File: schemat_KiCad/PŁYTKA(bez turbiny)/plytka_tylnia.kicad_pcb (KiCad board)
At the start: 2 copper layers, 200 x 150 mm, 80 parts, among them J1 CONN_01X04, J2 CONN_01X04, J3 CONN_01X04, J4 CONN_01X04, J5 CONN_01X04, J6 CONN_01X04, J7 PIN10, J8 CONN_01X04, J9 CONN_01X04, P1 USB_OTG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

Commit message: poprawiona, odchudzona, zaokraglona
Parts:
- moved R19 179.7 mm to (45.5, 65.0), turned to 90 degrees
- moved T5 179.7 mm to (45.5, 65.0), turned to 90 degrees
- moved R11 173.6 mm to (50.5, 68.0), turned to 90 degrees
- moved R15 160.5 mm to (60.5, 70.0), turned to 90 degrees
- moved T1 160.5 mm to (60.5, 70.0), turned to 90 degrees
- moved R1 154.0 mm to (66.0, 72.5), turned to 90 degrees
- moved R20 141.1 mm to (75.5, 72.5), turned to 90 degrees
- moved T6 141.1 mm to (75.5, 72.5), turned to 90 degrees
- moved J6 137.0 mm to (161.8, 163.2), turned to 0 degrees
- moved R12 136.3 mm to (80.0, 75.0), turned to 90 degrees
- moved C1.2 131.0 mm to (169.0, 158.8), turned to 270 degrees
- moved R16 127.1 mm to (89.0, 79.6), turned to 90 degrees
- moved U1 126.4 mm to (164.3, 155.7), turned to 270 degrees
- moved C15 123.7 mm to (169.0, 153.6), turned to 90 degrees
- moved T2 122.5 mm to (90.5, 75.0), turned to 90 degrees
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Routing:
- net GND: track 333.4 -> 356.9 mm, vias 5 -> 4
- net /GND1: track 84.5 -> 70.2 mm
- net /T2: track 70.0 -> 74.1 mm, vias 0 -> 1
- net /T1: track 95.3 -> 93.6 mm
- net VCC: track 569.1 -> 570.7 mm
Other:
- outline, holes or cut-outs redrawn

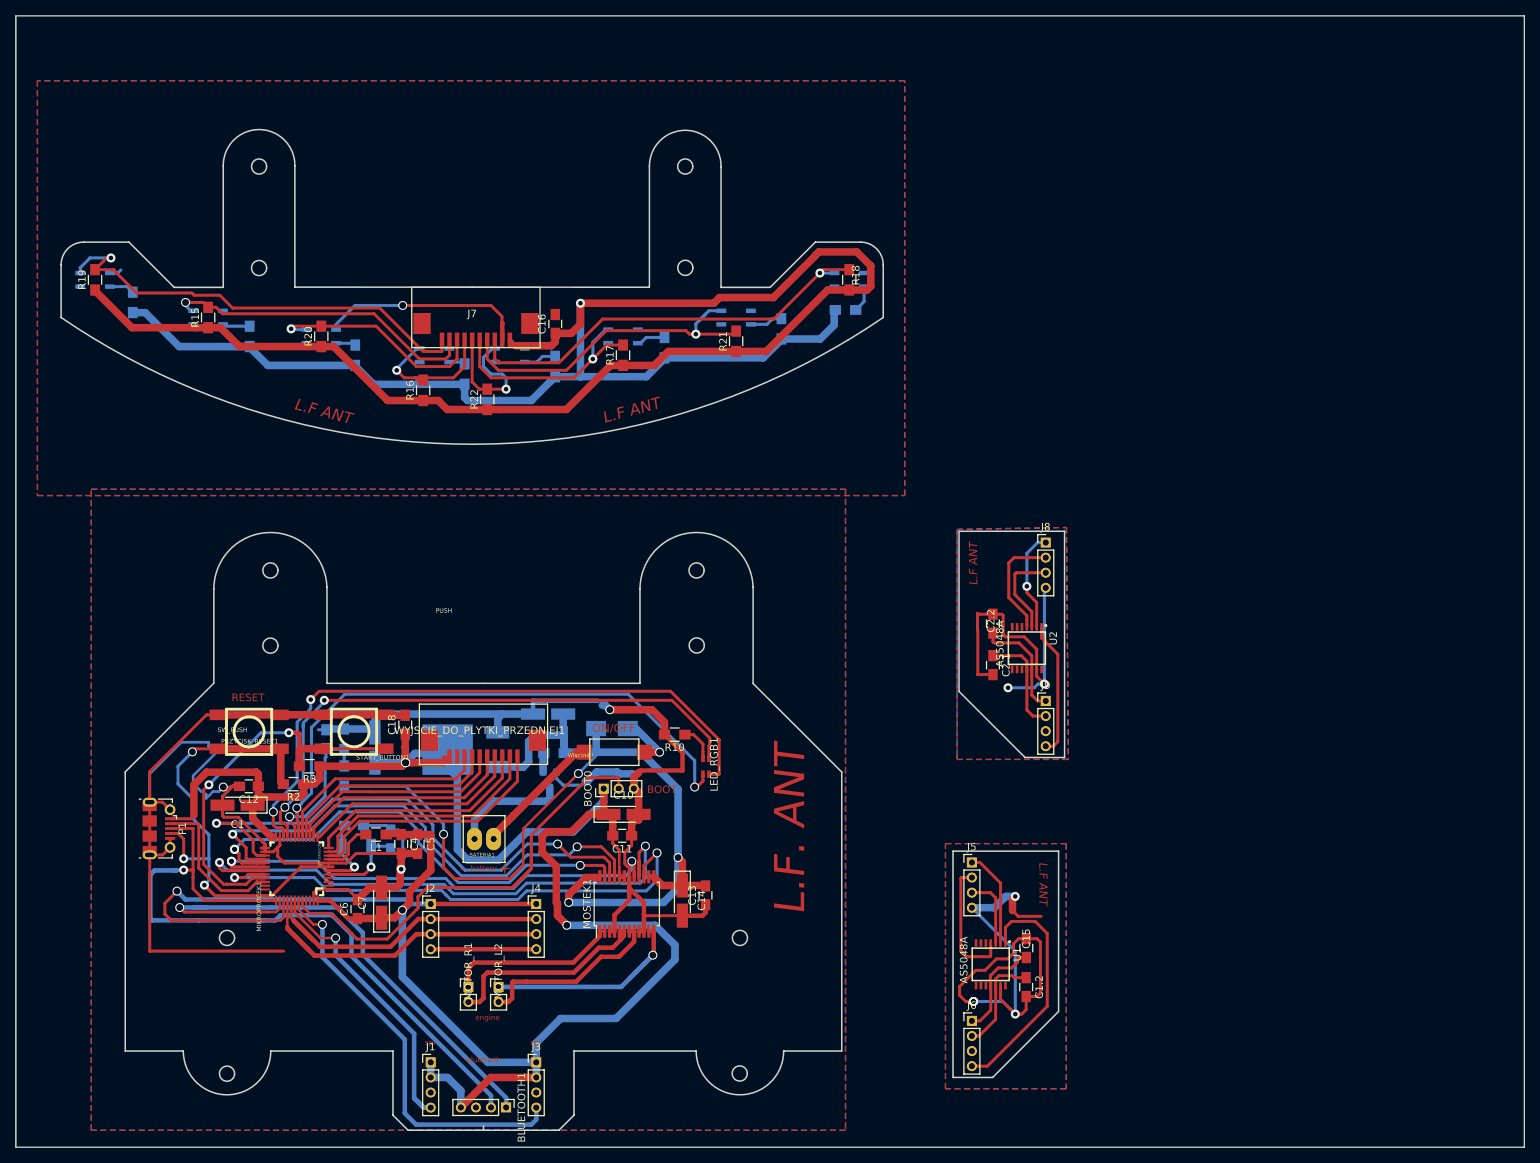
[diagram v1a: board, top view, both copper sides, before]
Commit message: zmniejszony obwod plytki
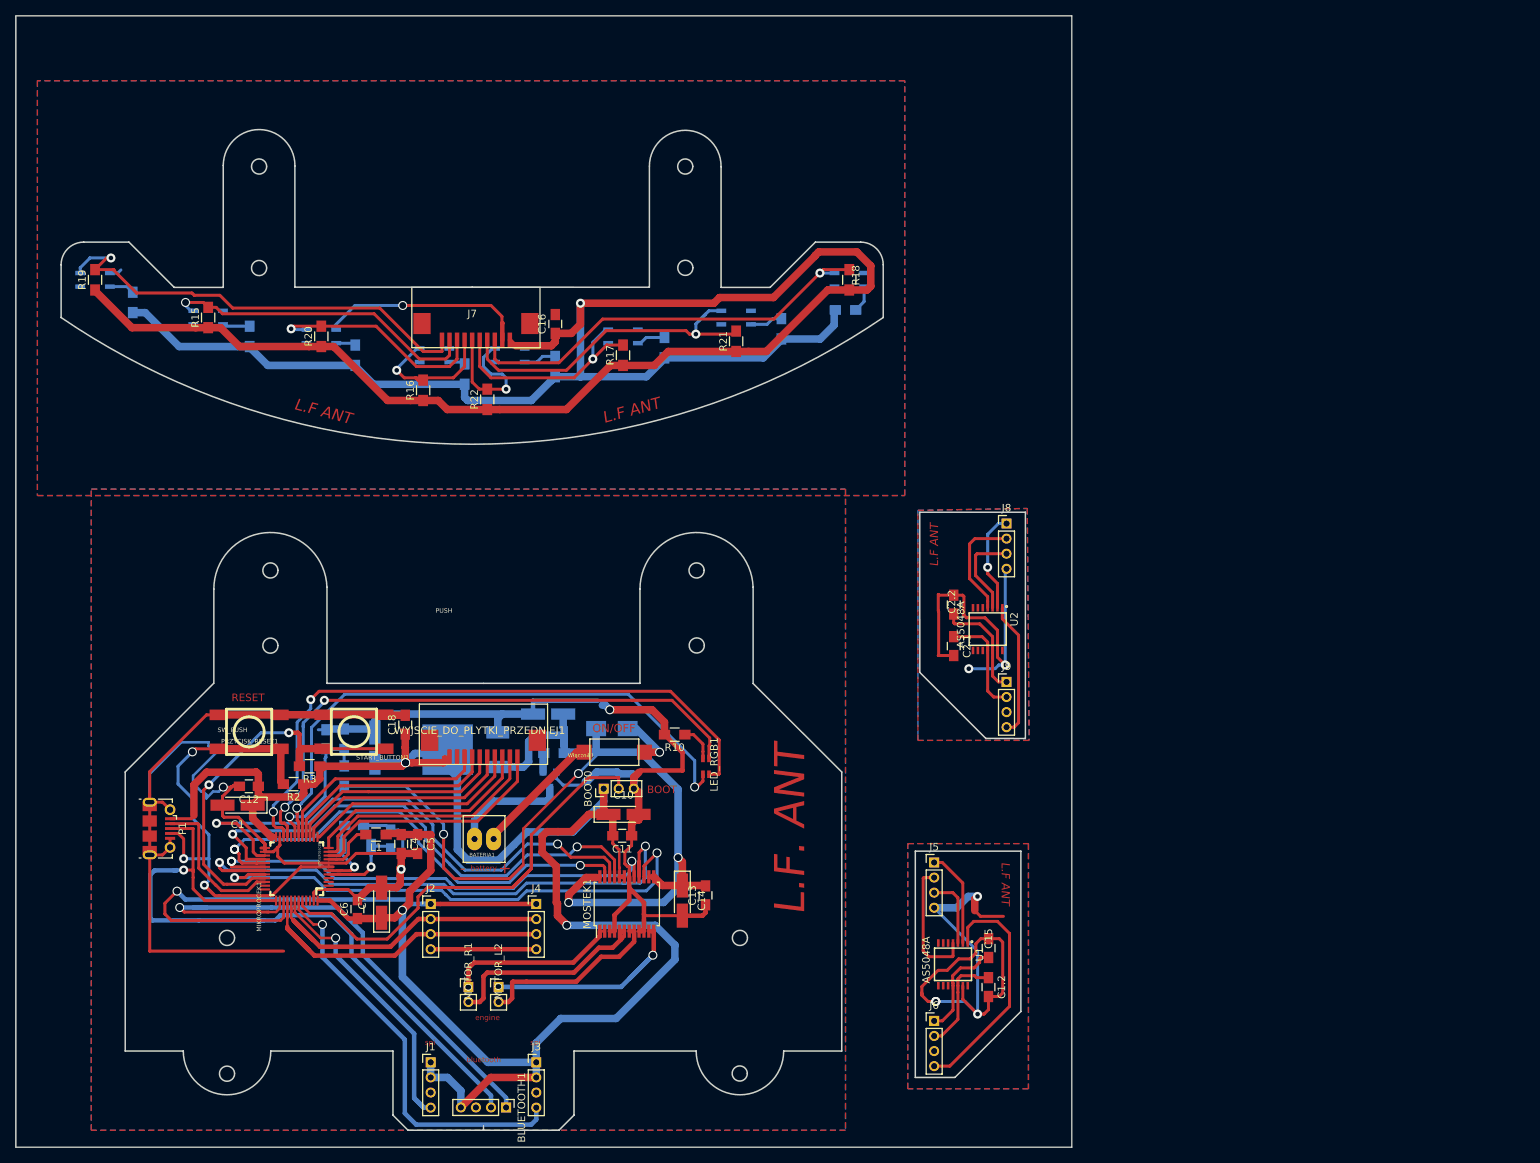
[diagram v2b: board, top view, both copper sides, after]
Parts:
- moved C2.1 5.78 mm to (159.3, 113.6)
- moved C2.2 5.78 mm to (159.3, 108.1)
- moved J8 5.78 mm to (166.3, 97.3)
- moved J9 5.78 mm to (166.3, 118.3)
- moved U2 5.78 mm to (163.8, 111.3)
- moved C1.2 5.00 mm to (164.0, 158.8)
- moved C15 5.00 mm to (164.0, 153.6)
- moved J5 5.00 mm to (156.8, 142.2)
- moved J6 5.00 mm to (156.8, 163.2)
- moved U1 5.00 mm to (159.3, 155.7)
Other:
- board size 200 x 150 mm -> 140 x 150 mm
